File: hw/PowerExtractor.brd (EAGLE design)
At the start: 74.6 x 77.5 mm, 86 parts, among them IC1 LM358D, Q1 BSS84, Q2 IRL530, Q4 BC847SMD, Q7 IRF530, T1 IRL530N, T2 IRF7416, U1 ZXCT1086E5TA, U2 ZXCT1086E5TA

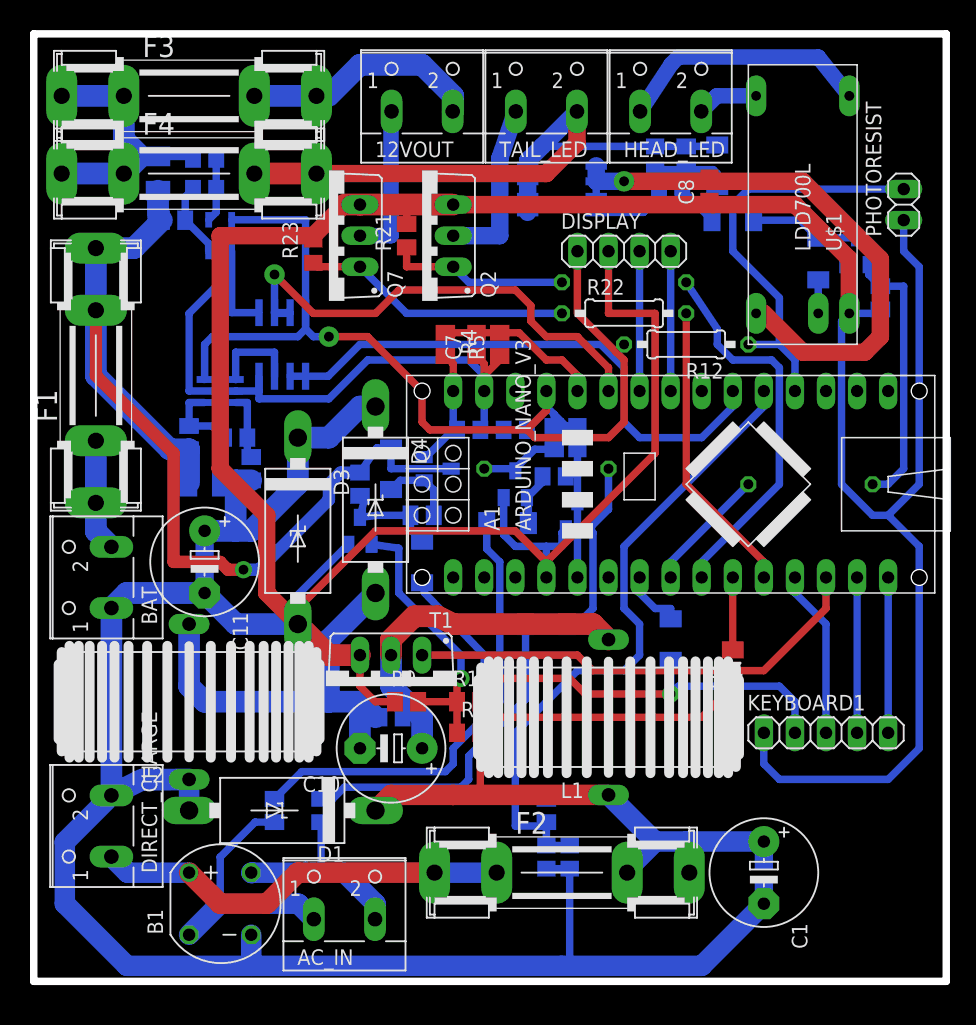
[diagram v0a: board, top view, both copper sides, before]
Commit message: Updated library - arduino removed holes from dimension layer
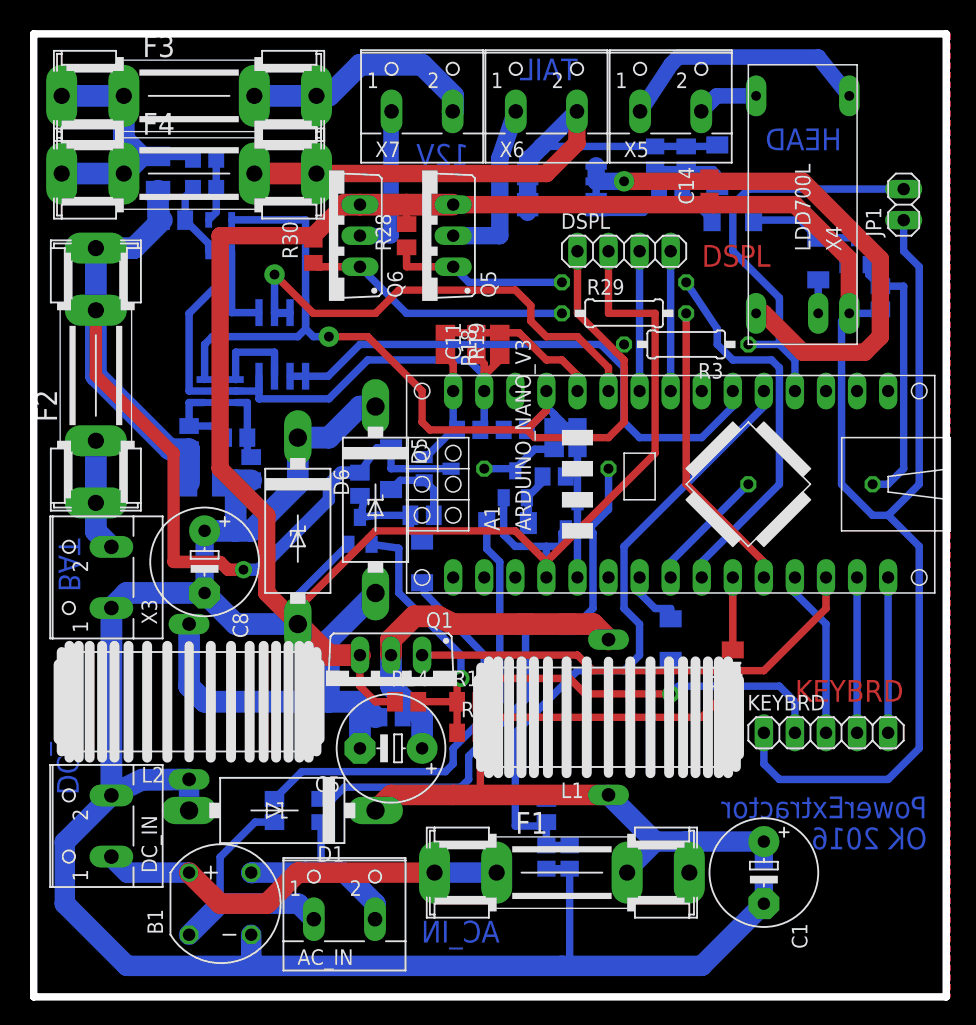
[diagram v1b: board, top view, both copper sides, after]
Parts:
- removed R31: 10k, rcl:M0805
- removed U$2, U$3: BCV47, triakcz:SOT23
- added Q3: BC847SMD, triakcz:SOT23
- added Q5: IRL530, transistor-power:TO220BV
- added R27: 2k2, rcl:0207/10
- B1: value (none) -> 1.5A
- C10: value 47uF/63V -> 100N; device rcl:E5-8,5 -> rcl:C0805
- C11: value 47uF/50V -> 10n; device rcl:E5-8,5 -> rcl:C0805
- C12, C7: value 10n -> 100N
- C13: value 100N -> 100n
- C14: value 1uF/50V -> 100n
- C4: value 1uF/50V -> 10n
- C5: value 100N -> 47uF/63V; device rcl:C0805 -> rcl:E5-8,5
- C6: value 100n -> 1uF/50V
- C8: value 100n -> 47uF/50V; device rcl:C0805 -> rcl:E5-8,5
- C9: value 100N -> 1uF/50V
- D10, D9: value 1N4148MINIMELF -> BZV55C15SMD; device triakcz:SOD80C -> diode:SOD80C
- D3: value 1N6267A -> 1N4148MINIMELF; device diode:C4111-15 -> triakcz:SOD80C
- D4: value SB360 -> 1N4148MINIMELF; device diode:C4111-15 -> triakcz:SOD80C
- D5: value BZV55C15SMD -> SB360; device diode:SOD80C -> diode:C4111-15
- D6: value BZV55C15SMD -> 1N6267A; device diode:SOD80C -> diode:C4111-15
- Q1: value BSS84 -> IRL530N; device triakcz:SOT23 -> transistor-power:TO220BV
- Q2: value IRL530 -> BSS84; device transistor-power:TO220BV -> triakcz:SOT23
- Q4: value BC847SMD -> IRF7416; device triakcz:SOT23 -> triakcz:SO-8
- R12: value 47k -> 10k; device rcl:0207/10 -> rcl:M0805
- R14: value 0R01 -> 47k; device rcl:M1206 -> rcl:M0805
- R16: value 10k -> 100k
- R17: value 100k -> 10k; device rcl:0207/10 -> rcl:M0805
- R18: value 100k -> 15k
- R19: value 330k -> 4k7
- R2: value 33K -> 330K; device rcl:R0805 -> rcl:M0805
- R20: value 2k2 -> 100k
- R22: value 2k2 -> 10k; device rcl:0207/10 -> rcl:M0805
- R23: value 100k -> 0R01; device rcl:R0805 -> rcl:M1206
- R24: value 330K -> 10k
- R25: value 330K -> 330k
- R26: value 100k -> 220R; device rcl:R0805 -> rcl:M0805
- R28: value 10k -> 100k; device rcl:R0805 -> rcl:M0805
- R29: value 10k -> 2k2; device rcl:M0805 -> rcl:0207/10
- R3: value 100k -> 47k; device rcl:M0805 -> rcl:0207/10
- R30, R6: value 10k -> 100k; device rcl:M0805 -> rcl:R0805
- R4: value 15k -> 10k
- R5: value 4k7 -> 100k; device rcl:M0805 -> rcl:0207/10
- R7: value 220R -> 10k; device rcl:M0805 -> rcl:R0805
- R8: value 100k -> 330K; device rcl:0207/10 -> rcl:M0805
- R9: value 47k -> 33K; device rcl:M0805 -> rcl:R0805
- T1: value IRL530N -> BCV47; device transistor-power:TO220BV -> triakcz:SOT23
- T2: value IRF7416 -> BCV47; device triakcz:SO-8 -> triakcz:SOT23
- moved C12 61.3 mm to (14.0, 68.6), turned to 0 degrees
- moved R25 61.1 mm to (53.3, 71.1), turned to 90 degrees
- moved F1 55.7 mm to (43.2, 12.7), turned to 0 degrees
- moved F2 55.7 mm to (5.08, 53.3), turned to 90 degrees
- moved R24 53.6 mm to (14.0, 71.1), turned to 180 degrees
- moved C8 51.3 mm to (14.0, 38.1), turned to 270 degrees
- moved C6 50.6 mm to (29.2, 25.4), turned to 0 degrees
- moved R14 47.7 mm to (30.5, 26.7), flipped to the top, turned to 0 degrees
- moved D8 40.8 mm to (31.8, 38.1), turned to 90 degrees
- moved D10 40.4 mm to (55.9, 70.5), turned to 270 degrees
- moved D5 39.1 mm to (27.9, 43.2), flipped to the top
- moved R21 39.1 mm to (69.2, 59.7), flipped to the bottom, turned to 270 degrees
- moved R22 37.6 mm to (11.4, 66.0), flipped to the bottom, turned to 180 degrees
- moved R12 37.0 mm to (17.8, 45.7), flipped to the bottom, turned to 90 degrees
- moved C4 36.9 mm to (41.9, 14.0), turned to 90 degrees
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- renumbered 12VOUT to X7, BAT to X3, DIRECT_CHARGE to DC_IN, DISPLAY to DSPL, HEAD_LED to X5, KEYBOARD1 to KEYBRD, PHOTORESIST to JP1, Q7 to Q6, TAIL_LED to X6, U$1 to X4, U$4 to T3
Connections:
- net +5V: now also C7.2, R3.2, R4.2, R7.2; no longer C13.2, R12.2, R28.2, R29.2
- net ARDUINO_LIGHT_IN: now also R3.1; no longer R12.1
- net ARDUINO_MAIN_LIGHT_CTRL: now also R20.2; no longer R17.2
- net ARDUINO_OUT_CHARGE_OUTPUT_CONTROL: now also R29.2; no longer R22.2
- net ARDUINO_OUT_TAIL_LIGHT: now also R27.2; no longer R20.2
- net ARDUINO_PWM_OUT: now also Q1.G; no longer T1.G
- net ARDUINO_ROTATION_INT: now also R6.1, R7.1, T2.3; no longer R26.1, R28.1, U$2.3
- net ARDUINO_SELF_POWER_OUT: now also D7.A; no longer D2.A
- net ARDUINO_VIN: now also C3.1, Q2.2, R18.2; no longer C14.1, Q1.2, R4.2
- net ARDUINO_VIN_ANALOG: now also C4.2, R8.1, R9.2; no longer C12.2, R1.1, R2.2
- net ARDUINO_VOUT_SENSE: now also C11.2, R18.1, R19.2; no longer C7.2, R4.1, R5.2
- net BAT+: now also F2.1A, F2.1B; no longer F1.1A, F1.1B
- net BAT+FUSED: now also D9.C, F2.2A, F2.2B, Q2.3, R16.2, R22.1, R23.1; no longer D6.C, F1.2A, F1.2B, Q1.3, R14.1, R3.2, R30.1
- net GND: now also C11.1, C14.1, C3.2, C4.1, C8.-, C9.2, D6.A, Q1.S, Q3.2, Q5.S, R14.1, R19.1, R28.2, R30.2, T1.2, T2.2; no longer C11.-, C12.1, C13.1, C14.2, C4.2, C8.1, D3.A, Q2.S, Q4.2, R18.2, R2.1, R23.2, R5.1, T1.S, U$2.2, U$3.2
- net HUB1: now also R1.2; no longer R24.2
- net HUB2: now also R2.2; no longer R25.2
- net LIGHTVCC: now also C13.2, D10.C, Q4.5, Q4.6, Q4.7, Q4.8, R25.2; no longer C6.2, D5.C, R19.2, T2.5, T2.6, T2.7, T2.8
- net N$1: now also C10.2, R12.2; no longer C5.2, R16.2
- net N$10: now also F1.1A, F1.1B; no longer F2.1A, F2.1B
- net N$12: now also D7.C; no longer D2.C
- net N$14: now also C13.1, D10.A, Q4.4, R25.1, R26.2; no longer C6.1, D5.A, R19.1, R7.2, T2.4
- net N$16: now also C10.1, R15.2; no longer C5.1, R30.2
- net N$17: now also Q3.1, R20.1, R21.1; no longer Q4.1, R17.1, R18.1
- net N$18: now also D11.A, R26.1; no longer D7.A, R7.1
- net N$19: now also C14.2, Q4.1, Q4.2, Q4.3; no longer C8.2, T2.1, T2.2, T2.3
- net N$2: now also C5.+, C6.1, Q1.D; no longer C10.+, C3.1, T1.D
- net N$20: now also D12.A; no longer D8.A
- net N$22: now also D8.A, R16.1, R17.2; no longer D10.A, R3.1, R6.2
- net N$24: now also Q5.G, R27.1, R28.1; no longer Q2.G, R20.1, R21.1
- net N$25: now also Q5.D; no longer Q2.D
- net N$27: now also R29.1, R30.1; no longer R22.1, R23.1
- net N$29: now also D2.A, R1.1; no longer D9.A, R24.1
- net N$3: now also C5.-, C6.2, D5.A; no longer C10.-, C3.2, D4.A
- net N$30: now also R4.1, R5.2, T1.3; no longer R29.1, R8.2, U$3.3
- net N$31: now also D2.C, R6.2, T1.1; no longer D9.C, R26.2, U$3.1
- net N$32: now also D3.C, R5.1, T2.1; no longer D11.C, R8.1, U$2.1
- net N$38: now also D3.A, R2.1; no longer D11.A, R25.1
- net N$4: now also R14.2; no longer R9.2
- net N$41: now also D4.A; no longer D12.A
- net N$46: now also C12.2, R22.2; no longer C9.2, R15.2
- net N$47: now also C12.1, R24.2; no longer C9.1, R31.2
- net N$6: now also D4.C, D8.C; no longer D10.C, D12.C
- net N$7: now also D9.A, Q2.1, R17.1; no longer D6.A, Q1.1, R6.1
- net N$9: now also D11.C, D12.C, Q3.3; no longer D7.C, D8.C, Q4.3
- net OUT+SENSED: now also R23.2, R24.1; no longer R14.2, R31.1
- net OUTPUT_TO_SENSE: now also C8.+, C9.1, D5.C, D6.C, R12.1; no longer C11.+, C4.1, D3.C, D4.C, R16.1
- net VIN: now also F1.2A, F1.2B, R8.2; no longer F2.2A, F2.2B, R1.2
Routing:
- added copper zone on layer 1, net GND
- added copper zone on layer 16, net GND
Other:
- board size 74.6 x 77.5 mm -> 74.6 x 78.7 mm
- board text added: "12V"
- board text added: "AC_IN"
- board text added: "BAT"
- board text added: "DC_IN"
- board text added: "DSPL"
- board text added: "HEAD"
- board text added: "KEYBRD"
- board text added: "OK 2016"
- board text added: "PowerExtractor"
- board text added: "TAIL"

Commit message: Fixed values and types of few parts
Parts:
- Q5: value IRL530 -> IRL530N
- Q6: value IRF530 -> IRL530N
- R14: value 47k -> 100k
- R18: value 15k -> 33k
- R19: value 4k7 -> 10k
- R26: value 220R -> 2k2
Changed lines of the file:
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@@
 <element name="B1" library="rectifier" package="RB1A" value="1.5A" x="15.24" y="10.16"/>
 <element name="D5" library="diode" package="C4111-15" value="SB360" x="27.94" y="43.18" rot="R270"/>
-<element name="R18" library="rcl" package="M0805" value="15k" x="33.655" y="55.88" rot="R270"/>
-<element name="R19" library="rcl" package="M0805" value="4k7" x="38.1" y="55.88" rot="R90"/>
+<element name="R18" library="rcl" package="M0805" value="33k" x="33.655" y="55.88" rot="R270"/>
+<element name="R19" library="rcl" package="M0805" value="10k" x="38.1" y="55.88" rot="R90"/>
 <element name="C11" library="rcl" package="C0805" value="10n" x="36.195" y="55.88" rot="R90"/>
 <element name="AC_IN" library="con-wago-500" package="W237-102" value="" x="25.4" y="10.16">
@@
 </element>
 <element name="Q2" library="triakcz" package="SOT23" value="BSS84" x="33.02" y="45.72" rot="MR90"/>
-<element name="R14" library="rcl" package="M0805" value="47k" x="30.48" y="26.67"/>
+<element name="R14" library="rcl" package="M0805" value="100k" x="30.48" y="26.67"/>
 <element name="X3" library="con-wago-500" package="W237-102" value="" x="5.08" y="36.83" rot="R90">
 <attribute name="OC_NEWARK" value="70K9898" x="80.01" y="64.77" size="1.778" layer="27" rot="R90" display="off"/>
@@
 <element name="R21" library="rcl" package="M0805" value="100k" x="69.215" y="59.69" rot="MR270"/>
 <element name="D10" library="diode" package="SOD80C" value="BZV55C15SMD" x="55.88" y="70.485" rot="MR270"/>
-<element name="R26" library="rcl" package="M0805" value="220R" x="52.07" y="67.945" rot="MR0"/>
+<element name="R26" library="rcl" package="M0805" value="2k2" x="52.07" y="67.945" rot="MR0"/>
 <element name="R25" library="rcl" package="M0805" value="330k" x="53.34" y="71.12" rot="MR90"/>
 <element name="C13" library="rcl" package="C0805" value="100n" x="50.8" y="71.12" rot="MR90"/>
@@
 <element name="C4" library="rcl" package="C0805" value="10n" x="41.91" y="13.97" rot="MR90"/>
 <element name="C3" library="rcl" package="C0805" value="1uF/50V" x="35.56" y="48.895" rot="MR180"/>
-<element name="Q5" library="transistor-power" package="TO220BV" value="IRL530" x="31.75" y="64.77" rot="R90"/>
-<element name="Q6" library="transistor-power" package="TO220BV" value="IRF530" x="24.13" y="64.77" rot="R90"/>
+<element name="Q5" library="transistor-power" package="TO220BV" value="IRL530N" x="31.75" y="64.77" rot="R90"/>
+<element name="Q6" library="transistor-power" package="TO220BV" value="IRL530N" x="24.13" y="64.77" rot="R90"/>
 <element name="JP1" library="pinhead" package="1X02" value="" x="71.12" y="67.31" rot="R90"/>
 <element name="T2" library="triakcz" package="SOT23" value="BCV47" x="44.45" y="41.91" rot="MR0"/>

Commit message: Fixed BSS84 pinout
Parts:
- moved Q2 1.80 mm to (31.8, 47.0), turned to 0 degrees
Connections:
- net ARDUINO_VIN: now also Q2.3; no longer Q2.2
- net BAT+FUSED: now also Q2.2; no longer Q2.3
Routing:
- net BAT+FUSED: track 85.3 -> 80.9 mm
- net N$7: track 6.20 -> 9.34 mm
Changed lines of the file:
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@@
 <attribute name="OC_FARNELL" value="unknown" x="68.58" y="-39.37" size="1.778" layer="27" display="off"/>
 </element>
-<element name="Q2" library="triakcz" package="SOT23" value="BSS84" x="33.02" y="45.72" rot="MR90"/>
 <element name="R14" library="rcl" package="M0805" value="100k" x="30.48" y="26.67"/>
 <element name="X3" library="con-wago-500" package="W237-102" value="" x="5.08" y="36.83" rot="R90">
@@
 <element name="D8" library="triakcz" package="SOD80C" value="1N4148MINIMELF" x="31.75" y="38.1" rot="MR90"/>
 <element name="D4" library="triakcz" package="SOD80C" value="1N4148MINIMELF" x="52.07" y="31.75" rot="MR90"/>
+<element name="Q2" library="triakcz" package="SOT23" value="BSS84" x="31.75" y="46.99" rot="MR0"/>
 </elements>
 <signals>
@@
 <signal name="ARDUINO_VIN">
 <contactref element="R18" pad="2"/>
-<contactref element="Q2" pad="2"/>
 <contactref element="A1" pad="VIN"/>
 <contactref element="C3" pad="1"/>
@@
 <wire x1="33.655" y1="54.93" x2="34.29" y2="54.295" width="0.6096" layer="1"/>
 <wire x1="34.29" y1="54.295" x2="34.29" y2="52.07" width="0.6096" layer="1"/>
-<wire x1="34.29" y1="48.895" x2="32.065" y2="46.67" width="0.6096" layer="16"/>
-<wire x1="32.065" y1="46.67" x2="31.92" y2="46.67" width="0.6096" layer="16"/>
+<contactref element="Q2" pad="3"/>
+<wire x1="31.75" y1="48.09" x2="33.805" y2="48.09" width="0.6096" layer="16"/>
+<wire x1="33.805" y1="48.09" x2="34.61" y2="48.895" width="0.6096" layer="16"/>
 </signal>
 <signal name="N$7">
@@
 <contactref element="R17" pad="1"/>
 <contactref element="Q2" pad="1"/>
-<wire x1="31.92" y1="44.77" x2="32.7" y2="43.99" width="0.6096" layer="16"/>
-<wire x1="32.7" y1="43.99" x2="32.7" y2="41.91" width="0.6096" layer="16"/>
-<wire x1="29.21" y1="44.02" x2="29.96" y2="44.77" width="0.6096" layer="16"/>
-<wire x1="29.96" y1="44.77" x2="31.92" y2="44.77" width="0.6096" layer="16"/>
+<wire x1="32.7" y1="45.89" x2="32.7" y2="41.91" width="0.6096" layer="16"/>
+<wire x1="29.21" y1="44.02" x2="32.7" y2="44.02" width="0.6096" layer="16"/>
+<wire x1="32.7" y1="44.02" x2="32.7" y2="45.89" width="0.6096" layer="16"/>
 </signal>
 <signal name="ARDUINO_SELF_POWER_OUT">
@@
 <contactref element="D9" pad="C"/>
 <contactref element="R16" pad="2"/>
-<contactref element="Q2" pad="3"/>
 <contactref element="F2" pad="2A"/>
 <contactref element="F2" pad="2B"/>
@@
 <wire x1="26.67" y1="45.4" x2="28.05" y2="47.42" width="0.6096" layer="16"/>
 <wire x1="28.05" y1="47.42" x2="29.21" y2="47.42" width="0.6096" layer="16"/>
-<wire x1="34.12" y1="45.72" x2="29.21" y2="45.72" width="0.6096" layer="16"/>
-<wire x1="29.21" y1="45.72" x2="29.21" y2="47.42" width="0.6096" layer="16"/>
 <wire x1="26.67" y1="45.4" x2="25.08" y2="45.4" width="1.016" layer="16"/>
 <wire x1="25.08" y1="45.4" x2="24.13" y2="44.45" width="1.016" layer="16"/>
@@
 <wire x1="11.43" y1="46.99" x2="5.08" y2="53.34" width="1.016" layer="1"/>
 <wire x1="5.08" y1="53.34" x2="5.08" y2="58.674" width="1.016" layer="1"/>
+<contactref element="Q2" pad="2"/>
+<wire x1="30.8" y1="45.89" x2="30.74" y2="45.89" width="0.6096" layer="16"/>
+<wire x1="30.74" y1="45.89" x2="29.21" y2="47.42" width="0.6096" layer="16"/>
 </signal>
 <signal name="N$5">

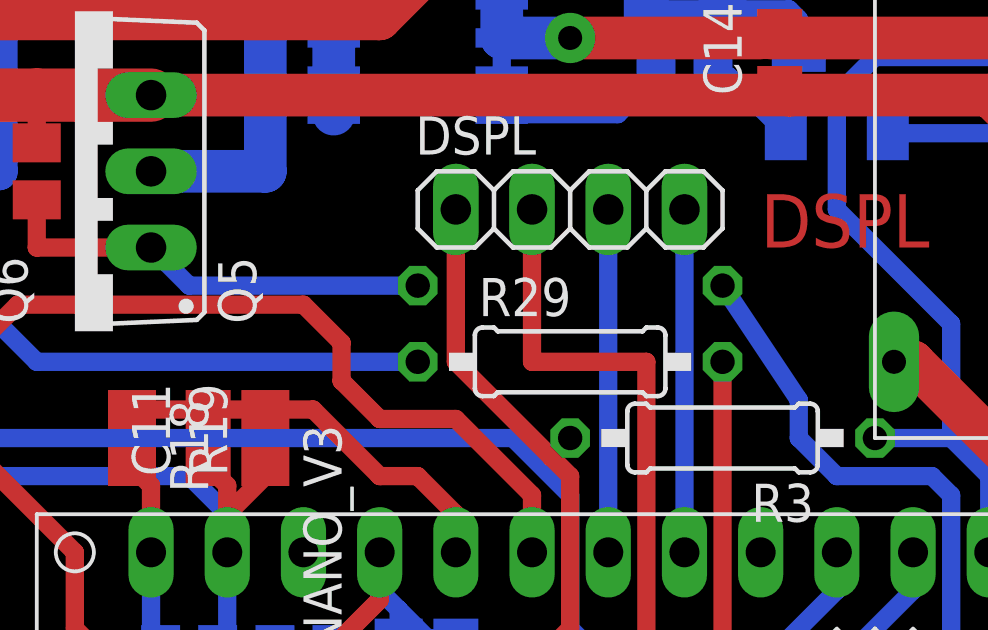
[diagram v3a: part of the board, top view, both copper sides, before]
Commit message: Fixed wrongly placed resistor (0207 placed on bottom side)
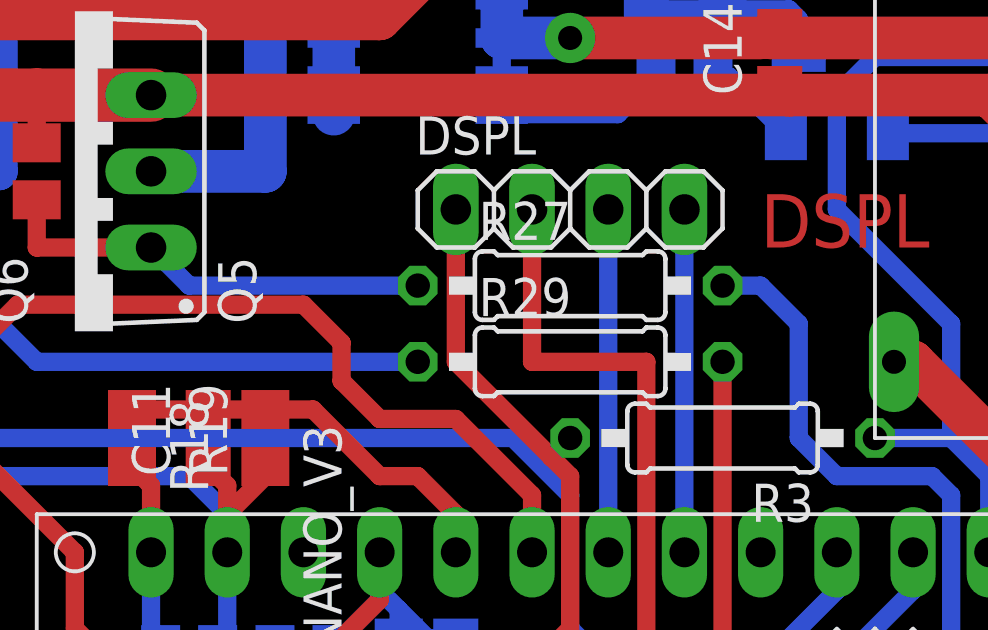
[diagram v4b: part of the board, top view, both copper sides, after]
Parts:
- flipped R27 to the top, turned to 0 degrees
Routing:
- net ARDUINO_OUT_TAIL_LIGHT: track 31.5 -> 32.5 mm
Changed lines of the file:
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@@
 </element>
 <element name="C14" library="rcl" package="C0805" value="100n" x="55.245" y="68.58" rot="R90"/>
-<element name="R27" library="rcl" package="0207/10" value="2k2" x="48.26" y="60.96" rot="MR180"/>
+<element name="R27" library="rcl" package="0207/10" value="2k2" x="48.26" y="60.96"/>
 <element name="R28" library="rcl" package="M0805" value="100k" x="30.48" y="64.77" rot="R90"/>
 <element name="X6" library="con-wago-500" package="W237-102" value="" x="41.91" y="76.2">
@@
 <wire x1="30.48" y1="63.82" x2="30.48" y2="62.23" width="0.6096" layer="1"/>
 <wire x1="30.48" y1="62.23" x2="34.29" y2="62.23" width="0.6096" layer="1"/>
-<wire x1="43.18" y1="60.96" x2="35.56" y2="60.96" width="0.6096" layer="16"/>
 <wire x1="35.56" y1="60.96" x2="34.29" y2="62.23" width="0.6096" layer="16"/>
+<wire x1="35.56" y1="60.96" x2="43.18" y2="60.96" width="0.6096" layer="16"/>
 </signal>
 <signal name="ARDUINO_OUT_TAIL_LIGHT">
 <contactref element="R27" pad="2"/>
 <contactref element="A1" pad="D6"/>
-<wire x1="53.34" y1="60.96" x2="55.88" y2="57.15" width="0.6096" layer="16"/>
-<wire x1="55.88" y1="57.15" x2="55.88" y2="55.88" width="0.6096" layer="16"/>
 <wire x1="55.88" y1="55.88" x2="57.15" y2="54.61" width="0.6096" layer="16"/>
 <wire x1="57.15" y1="54.61" x2="60.325" y2="54.61" width="0.6096" layer="16"/>
@@
 <wire x1="60.96" y1="44.45" x2="54.61" y2="38.1" width="0.6096" layer="16"/>
 <wire x1="54.61" y1="38.1" x2="54.61" y2="36.83" width="0.6096" layer="16"/>
+<wire x1="55.88" y1="55.88" x2="55.88" y2="59.69" width="0.6096" layer="16"/>
+<wire x1="55.88" y1="59.69" x2="54.61" y2="60.96" width="0.6096" layer="16"/>
+<wire x1="54.61" y1="60.96" x2="53.34" y2="60.96" width="0.6096" layer="16"/>
 </signal>
 <signal name="N$25">
